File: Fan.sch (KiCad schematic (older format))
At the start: 0 parts

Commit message: Completed LED Driver Video + Power Module
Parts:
- added Q?: MOSFET_N, ~, symbol MOSFET_N
- added R? (x5): R, ~, symbol R
- added RV?: POT, ~, symbol POT
- added U?: LM324, symbol LM324
- added U?: MCP4922-E/P, DIP14, symbol MCP4922-E/P
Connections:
- net labels added: +12V, -12V, AGND, CS_N, Current Measure, MISO, MOSI, SCLK
- wire segments 0 -> 32
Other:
- note added: "NEED TO CHANGE CS NAME, THIS WILL DUPLICATE WITH THE OTHER CS ON TC"

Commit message: Completed Arduino Module Video
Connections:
- net labels added: CURR_MEAS, FAN_EN_N, FAN_OUT+, FAN_OUT-, TACH_IN, TACH_MEAS
- net labels removed: Current Measure, Fan_In, Power+, Power-, Tach, Tach_Out
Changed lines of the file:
@@
 $Descr A4 11693 8268
 encoding utf-8
-Sheet 7 9
+Sheet 8 9
 Title ""
-Date "10 feb 2014"
+Date "11 feb 2014"
 Rev ""
 Comp ""
@@
 $EndDescr
 Text HLabel 8900 3500 2    60   Output ~ 0
-Power+
-Text HLabel 8900 4000 2    60   Input ~ 0
-Power-
+FAN_OUT+
+Text HLabel 8900 4000 2    60   Output ~ 0
+FAN_OUT-
 Text HLabel 9000 5900 2    60   Input ~ 0
-Tach
+TACH_IN
 Text HLabel 1900 5900 0    60   Output ~ 0
-Tach_Out
+TACH_MEAS
 Text HLabel 1850 4350 0    60   Input ~ 0
-Fan_In
+FAN_EN_N
 $Comp
 L LM324 U?
@@
 Connection ~ 4800 3950
 Text HLabel 2300 4750 0    60   Output ~ 0
-Current Measure
+CURR_MEAS
 Wire Wire Line
 	2300 4750 7950 4750

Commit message: Fan Module Update
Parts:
- removed R? (x2): R, ~, symbol R
- removed RV?: POT, ~, symbol POT
- added D?: DIODE, ~, symbol DIODE
- added Q? (x2): MOSFET_N, ~, symbol MOSFET_N
- added TH?: THERMISTOR, ~, symbol THERMISTOR
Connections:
- net labels added: +12C, FAN_MODE, FAN_PWM
- net labels removed: FAN_EN_N
- wire segments 32 -> 42
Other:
- moved on the sheet: R?
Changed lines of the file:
@@
 Comment4 ""
 $EndDescr
-Text HLabel 8900 3500 2    60   Output ~ 0
+Text HLabel 9450 2350 2    60   Output ~ 0
 FAN_OUT+
-Text HLabel 8900 4000 2    60   Output ~ 0
+Text HLabel 9450 2950 2    60   Output ~ 0
 FAN_OUT-
-Text HLabel 9000 5900 2    60   Input ~ 0
+Text HLabel 8900 6950 2    60   Input ~ 0
 TACH_IN
-Text HLabel 1900 5900 0    60   Output ~ 0
+Text HLabel 1800 6950 0    60   Output ~ 0
 TACH_MEAS
 Text HLabel 1850 4350 0    60   Input ~ 0
-FAN_EN_N
+FAN_PWM
 $Comp
 L LM324 U?
@@
 $EndComp
 $Comp
-L +12V #PWR?
-U 1 1 52F64FC8
-P 7950 2450
-F 0 "#PWR?" H 7950 2400 20  0001 C CNN
-F 1 "+12V" H 7950 2550 30  0000 C CNN
-F 2 "" H 7950 2450 60  0000 C CNN
-F 3 "" H 7950 2450 60  0000 C CNN
-	1    7950 2450
-	1    0    0    -1
-$EndComp
-$Comp
 L AGND #PWR?
 U 1 1 52F64FE1
-P 7950 5600
-F 0 "#PWR?" H 7950 5600 40  0001 C CNN
-F 1 "AGND" H 7950 5530 50  0000 C CNN
-F 2 "" H 7950 5600 60  0000 C CNN
-F 3 "" H 7950 5600 60  0000 C CNN
-	1    7950 5600
+P 7950 6100
+F 0 "#PWR?" H 7950 6100 40  0001 C CNN
+F 1 "AGND" H 7950 6030 50  0000 C CNN
+F 2 "" H 7950 6100 60  0000 C CNN
+F 3 "" H 7950 6100 60  0000 C CNN
+	1    7950 6100
 	1    0    0    -1
 $EndComp
@@
 	7650 3250 6950 3250
 Wire Wire Line
-	7950 3450 7950 3500
-Wire Wire Line
-	7950 3500 8900 3500
-Wire Wire Line
-	5750 4000 8900 4000
-Wire Wire Line
-	7950 4000 7950 4900
+	7950 3450 7950 4000
+Wire Wire Line
+	7950 4000 7950 4750
+Wire Wire Line
+	7950 4750 7950 5000
+Wire Wire Line
+	7950 5000 7950 5150
 $Comp
 L R R?
 U 1 1 52F65013
-P 7950 5150
-F 0 "R?" V 8030 5150 40  0000 C CNN
-F 1 "R" V 7957 5151 40  0000 C CNN
-F 2 "~" V 7880 5150 30  0000 C CNN
-F 3 "~" H 7950 5150 30  0000 C CNN
-	1    7950 5150
-	1    0    0    -1
-$EndComp
-Wire Wire Line
-	7950 5400 7950 5600
-Wire Wire Line
-	7950 3050 7950 2450
+P 7950 5400
+F 0 "R?" V 8030 5400 40  0000 C CNN
+F 1 "R" V 7957 5401 40  0000 C CNN
+F 2 "~" V 7880 5400 30  0000 C CNN
+F 3 "~" H 7950 5400 30  0000 C CNN
+	1    7950 5400
+	1    0    0    -1
+$EndComp
+Wire Wire Line
+	7950 5650 7950 5850
+Wire Wire Line
+	7950 5850 7950 6100
 Wire Wire Line
 	5750 4000 5750 3350
 Wire Wire Line
 	5750 3350 5950 3350
-Connection ~ 7950 4000
 $Comp
 L +12V #PWR?
@@
 $EndComp
 $Comp
-L R R?
-U 1 1 52F651D7
-P 4800 2800
-F 0 "R?" V 4880 2800 40  0000 C CNN
-F 1 "R" V 4807 2801 40  0000 C CNN
-F 2 "~" V 4730 2800 30  0000 C CNN
-F 3 "~" H 4800 2800 30  0000 C CNN
-	1    4800 2800
-	1    0    0    -1
-$EndComp
-Wire Wire Line
-	4800 3050 4800 3350
-$Comp
-L +12V #PWR?
-U 1 1 52F651EE
-P 4800 2450
-F 0 "#PWR?" H 4800 2400 20  0001 C CNN
-F 1 "+12V" H 4800 2550 30  0000 C CNN
-F 2 "" H 4800 2450 60  0000 C CNN
-F 3 "" H 4800 2450 60  0000 C CNN
-	1    4800 2450
-	1    0    0    -1
-$EndComp
-Wire Wire Line
-	4800 2550 4800 2450
-$Comp
-L POT RV?
-U 1 1 52F65207
-P 4800 3600
-F 0 "RV?" H 4800 3500 50  0000 C CNN
-F 1 "POT" H 4800 3600 50  0000 C CNN
-F 2 "~" H 4800 3600 60  0000 C CNN
-F 3 "~" H 4800 3600 60  0000 C CNN
-	1    4800 3600
-	0    1    1    0
-$EndComp
-$Comp
 L AGND #PWR?
 U 1 1 52F6521E
-P 4800 4150
-F 0 "#PWR?" H 4800 4150 40  0001 C CNN
-F 1 "AGND" H 4800 4080 50  0000 C CNN
-F 2 "" H 4800 4150 60  0000 C CNN
-F 3 "" H 4800 4150 60  0000 C CNN
-	1    4800 4150
-	1    0    0    -1
-$EndComp
-Wire Wire Line
-	4800 3850 4800 4150
-Connection ~ 4800 3150
-Wire Wire Line
-	4950 3600 5050 3600
-Wire Wire Line
-	5050 3600 5050 3950
-Wire Wire Line
-	5050 3950 4800 3950
-Connection ~ 4800 3950
-Text HLabel 2300 4750 0    60   Output ~ 0
+P 5100 4150
+F 0 "#PWR?" H 5100 4150 40  0001 C CNN
+F 1 "AGND" H 5100 4080 50  0000 C CNN
+F 2 "" H 5100 4150 60  0000 C CNN
+F 3 "" H 5100 4150 60  0000 C CNN
+	1    5100 4150
+	1    0    0    -1
+$EndComp
+Text HLabel 1850 4750 0    60   Output ~ 0
 CURR_MEAS
 Wire Wire Line
-	2300 4750 7950 4750
+	1850 4750 7950 4750
 Connection ~ 7950 4750
 Text HLabel 1150 3100 0    60   Input ~ 0
@@
 NEED TO CHANGE CS NAME,  THIS WILL DUPLICATE WITH THE OTHER CS ON TC
 Wire Wire Line
-	1900 5900 9000 5900
+	1800 6950 8900 6950
 $Comp
 L R R?
@@
 Wire Wire Line
 	1850 4350 2850 4350
-Wire Wire Line
-	5400 4350 3350 4350
-Connection ~ 5400 3150
 $Comp
 L R R?
@@
 	3150 3150 3750 3150
 Wire Wire Line
-	4250 3150 5950 3150
-Wire Wire Line
-	5400 3150 5400 4350
-$Comp
-L R R?
-U 1 1 52F654DF
-P 1950 3950
-F 0 "R?" V 2030 3950 40  0000 C CNN
-F 1 "R" V 1957 3951 40  0000 C CNN
-F 2 "~" V 1880 3950 30  0000 C CNN
-F 3 "~" H 1950 3950 30  0000 C CNN
-	1    1950 3950
-	-1   0    0    1
-$EndComp
-Wire Wire Line
-	1950 3700 1950 3500
-Wire Wire Line
-	1950 3500 2050 3500
-Wire Wire Line
-	1950 4200 1950 4350
-Connection ~ 1950 4350
+	4250 3150 5100 3150
+Wire Wire Line
+	5100 3150 5950 3150
+$Comp
+L THERMISTOR TH?
+U 1 1 52FA45CA
+P 7950 2050
+F 0 "TH?" V 8050 2100 50  0000 C CNN
+F 1 "THERMISTOR" V 7850 2050 50  0000 C CNN
+F 2 "~" H 7950 2050 60  0000 C CNN
+F 3 "~" H 7950 2050 60  0000 C CNN
+	1    7950 2050
+	1    0    0    -1
+$EndComp
+Wire Wire Line
+	7950 1800 7950 1600
+Wire Wire Line
+	7950 2300 7950 2350
+Wire Wire Line
+	7550 2350 7950 2350
+Wire Wire Line
+	7950 2350 9450 2350
+Wire Wire Line
+	7550 2950 7950 2950
+Wire Wire Line
+	7950 2950 9450 2950
+Wire Wire Line
+	7950 2950 7950 3050
+$Comp
+L DIODE D?
+U 1 1 52FA4653
+P 7550 2650
+F 0 "D?" H 7550 2750 40  0000 C CNN
+F 1 "DIODE" H 7550 2550 40  0000 C CNN
+F 2 "~" H 7550 2650 60  0000 C CNN
+F 3 "~" H 7550 2650 60  0000 C CNN
+	1    7550 2650
+	0    -1   -1   0
+$EndComp
+Wire Wire Line
+	7550 2850 7550 2950
+Connection ~ 7950 2950
+Wire Wire Line
+	7550 2450 7550 2350
+Connection ~ 7950 2350
+$Comp
+L MOSFET_N Q?
+U 1 1 52FA4715
+P 7300 5400
+F 0 "Q?" H 7310 5570 60  0000 R CNN
+F 1 "MOSFET_N" H 7310 5250 60  0000 R CNN
+F 2 "~" H 7300 5400 60  0000 C CNN
+F 3 "~" H 7300 5400 60  0000 C CNN
+	1    7300 5400
+	1    0    0    -1
+$EndComp
+Wire Wire Line
+	7400 5200 7400 5000
+Wire Wire Line
+	7400 5000 7950 5000
+Connection ~ 7950 5000
+Wire Wire Line
+	7400 5600 7400 5850
+Wire Wire Line
+	7400 5850 7950 5850
+Connection ~ 7950 5850
+Wire Wire Line
+	5750 4000 7950 4000
+Connection ~ 7950 4000
+$Comp
+L MOSFET_N Q?
+U 1 1 52FA47D3
+P 5000 3700
+F 0 "Q?" H 5010 3870 60  0000 R CNN
+F 1 "MOSFET_N" H 5010 3550 60  0000 R CNN
+F 2 "~" H 5000 3700 60  0000 C CNN
+F 3 "~" H 5000 3700 60  0000 C CNN
+	1    5000 3700
+	1    0    0    -1
+$EndComp
+Wire Wire Line
+	5100 3500 5100 3150
+Connection ~ 5100 3150
+Wire Wire Line
+	5100 3900 5100 4150
+Wire Wire Line
+	3350 4350 4000 4350
+Wire Wire Line
+	4000 4350 4000 3700
+Wire Wire Line
+	4000 3700 4800 3700
+Text HLabel 1850 5400 0    60   Input ~ 0
+FAN_MODE
+Wire Wire Line
+	1850 5400 7100 5400
+$Comp
+L +12C #PWR?
+U 1 1 52FA51D6
+P 7950 1600
+F 0 "#PWR?" H 7950 1570 30  0001 C CNN
+F 1 "+12C" H 7950 1710 40  0000 C CNN
+F 2 "" H 7950 1600 60  0000 C CNN
+F 3 "" H 7950 1600 60  0000 C CNN
+	1    7950 1600
+	1    0    0    -1
+$EndComp
 $EndSCHEMATC

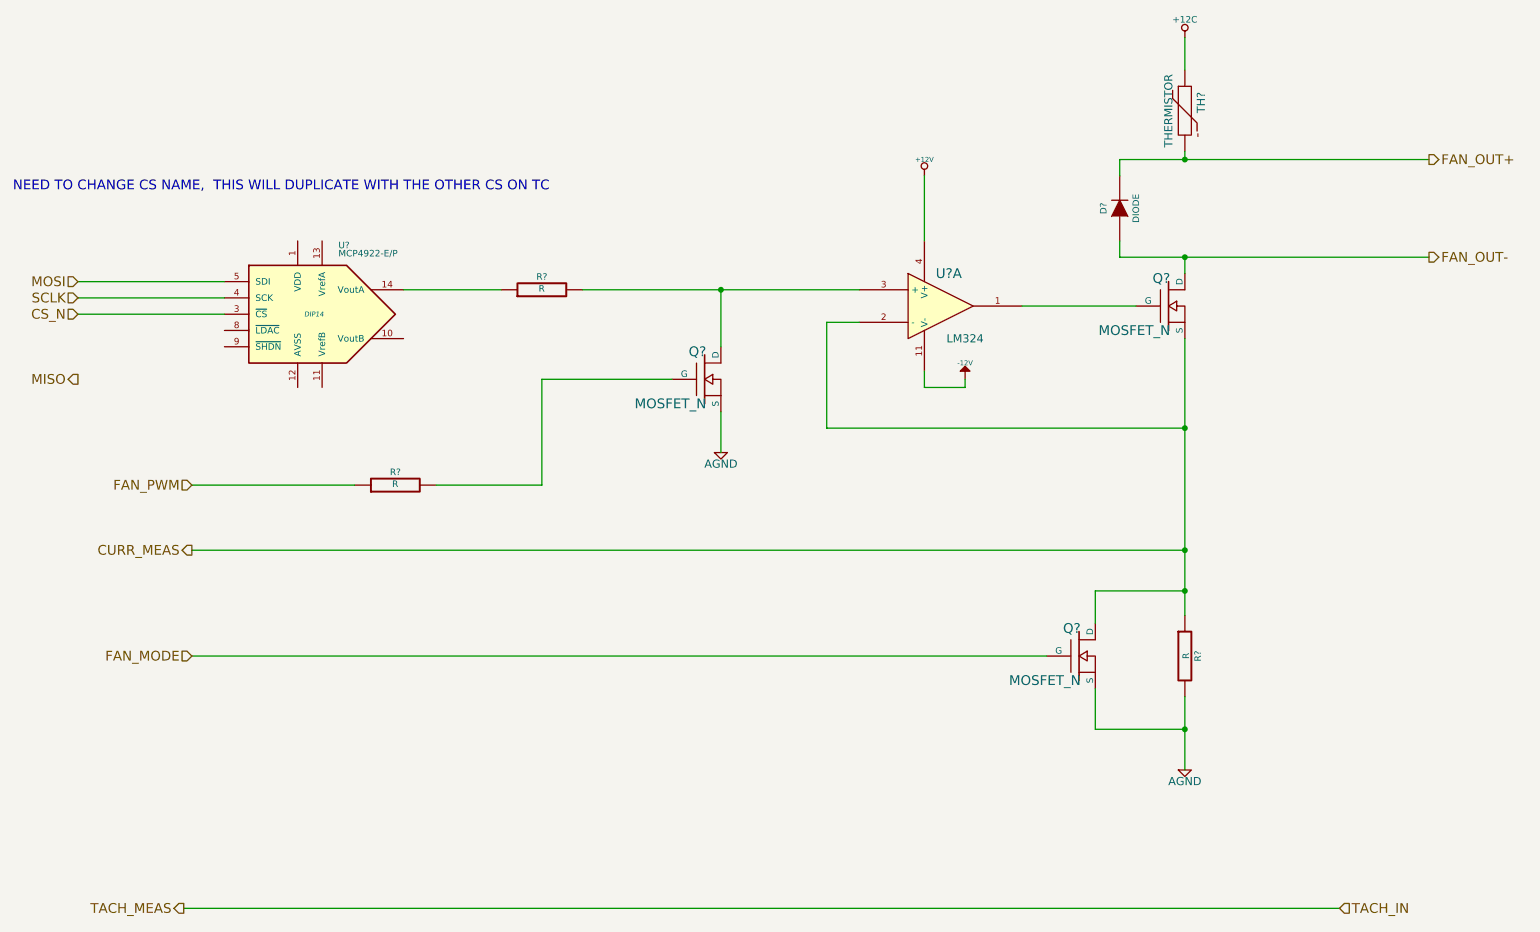
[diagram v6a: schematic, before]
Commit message: started associating relay parts
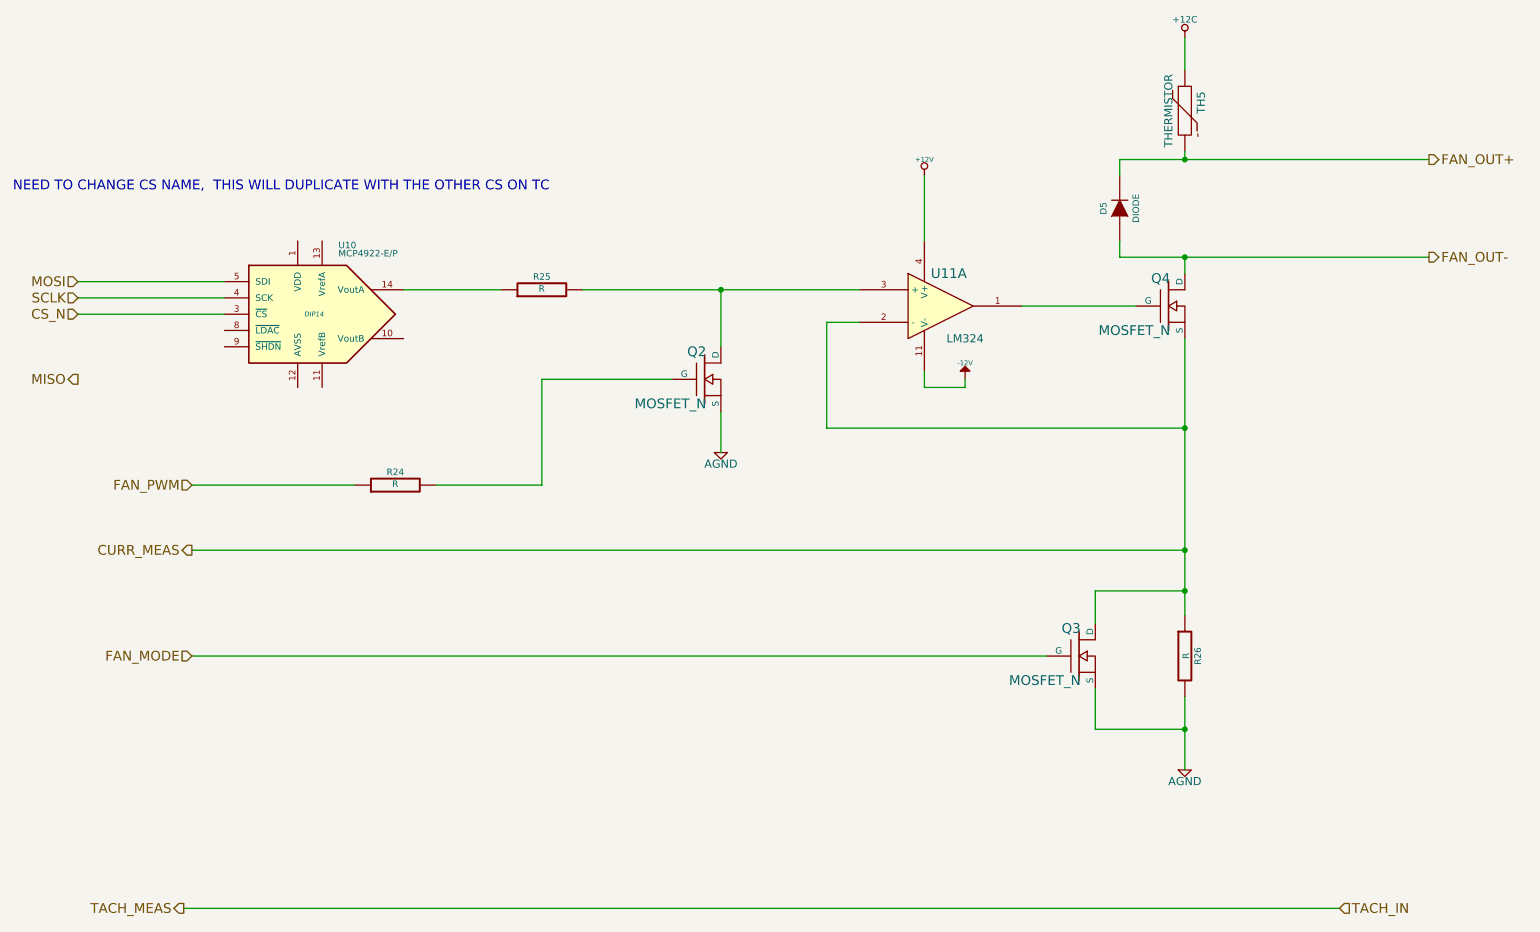
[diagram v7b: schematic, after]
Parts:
- gave numbers to parts that had none: 10
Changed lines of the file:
@@
 Sheet 8 9
 Title ""
-Date "17 feb 2014"
+Date "20 feb 2014"
 Rev ""
 Comp ""
@@
 FAN_PWM
 $Comp
-L LM324 U?
+L LM324 U11
 U 1 1 52F64FAA
 P 6450 3250
-F 0 "U?" H 6500 3450 60  0000 C CNN
+F 0 "U11" H 6500 3450 60  0000 C CNN
 F 1 "LM324" H 6600 3050 50  0000 C CNN
 F 2 "" H 6450 3250 60  0000 C CNN
@@
 $EndComp
 $Comp
-L MOSFET_N Q?
+L MOSFET_N Q4
 U 1 1 52F64FB9
 P 7850 3250
-F 0 "Q?" H 7860 3420 60  0000 R CNN
+F 0 "Q4" H 7860 3420 60  0000 R CNN
 F 1 "MOSFET_N" H 7860 3100 60  0000 R CNN
 F 2 "~" H 7850 3250 60  0000 C CNN
@@
 $EndComp
 $Comp
-L AGND #PWR?
+L AGND #PWR041
 U 1 1 52F64FE1
 P 7950 6100
-F 0 "#PWR?" H 7950 6100 40  0001 C CNN
+F 0 "#PWR041" H 7950 6100 40  0001 C CNN
 F 1 "AGND" H 7950 6030 50  0000 C CNN
 F 2 "" H 7950 6100 60  0000 C CNN
@@
 	7650 3250 6950 3250
 Wire Wire Line
-	7950 3450 7950 4000
-Wire Wire Line
-	7950 4000 7950 4750
-Wire Wire Line
-	7950 4750 7950 5000
-Wire Wire Line
-	7950 5000 7950 5150
-$Comp
-L R R?
+	7950 3450 7950 5150
+$Comp
+L R R26
 U 1 1 52F65013
 P 7950 5400
-F 0 "R?" V 8030 5400 40  0000 C CNN
+F 0 "R26" V 8030 5400 40  0000 C CNN
 F 1 "R" V 7957 5401 40  0000 C CNN
 F 2 "~" V 7880 5400 30  0000 C CNN
@@
 $EndComp
 Wire Wire Line
-	7950 5650 7950 5850
-Wire Wire Line
-	7950 5850 7950 6100
+	7950 5650 7950 6100
 Wire Wire Line
 	5750 4000 5750 3350
@@
 	5750 3350 5950 3350
 $Comp
-L +12V #PWR?
+L +12V #PWR042
 U 1 1 52F65053
 P 6350 2450
-F 0 "#PWR?" H 6350 2400 20  0001 C CNN
+F 0 "#PWR042" H 6350 2400 20  0001 C CNN
 F 1 "+12V" H 6350 2550 30  0000 C CNN
 F 2 "" H 6350 2450 60  0000 C CNN
@@
 	6350 2450 6350 2850
 $Comp
-L -12V #PWR?
+L -12V #PWR043
 U 1 1 52F65100
 P 6600 3700
-F 0 "#PWR?" H 6600 3830 20  0001 C CNN
+F 0 "#PWR043" H 6600 3830 20  0001 C CNN
 F 1 "-12V" H 6600 3800 30  0000 C CNN
 F 2 "" H 6600 3700 60  0000 C CNN
@@
 	6600 3750 6600 3700
 $Comp
-L MCP4922-E/P U?
+L MCP4922-E/P U10
 U 1 1 52F651B6
 P 2600 3300
-F 0 "U?" H 2750 3700 40  0000 L BNN
+F 0 "U10" H 2750 3700 40  0000 L BNN
 F 1 "MCP4922-E/P" H 2750 3650 40  0000 L BNN
 F 2 "DIP14" H 2600 3300 30  0000 C CIN
@@
 $EndComp
 $Comp
-L AGND #PWR?
+L AGND #PWR044
 U 1 1 52F6521E
 P 5100 4150
-F 0 "#PWR?" H 5100 4150 40  0001 C CNN
+F 0 "#PWR044" H 5100 4150 40  0001 C CNN
 F 1 "AGND" H 5100 4080 50  0000 C CNN
 F 2 "" H 5100 4150 60  0000 C CNN
@@
 	1800 6950 8900 6950
 $Comp
-L R R?
+L R R24
 U 1 1 52F65324
 P 3100 4350
-F 0 "R?" V 3180 4350 40  0000 C CNN
+F 0 "R24" V 3180 4350 40  0000 C CNN
 F 1 "R" V 3107 4351 40  0000 C CNN
 F 2 "~" V 3030 4350 30  0000 C CNN
@@
 	1850 4350 2850 4350
 $Comp
-L R R?
+L R R25
 U 1 1 52F6536C
 P 4000 3150
-F 0 "R?" V 4080 3150 40  0000 C CNN
+F 0 "R25" V 4080 3150 40  0000 C CNN
 F 1 "R" V 4007 3151 40  0000 C CNN
 F 2 "~" V 3930 3150 30  0000 C CNN
@@
 	3150 3150 3750 3150
 Wire Wire Line
-	4250 3150 5100 3150
-Wire Wire Line
-	5100 3150 5950 3150
-$Comp
-L THERMISTOR TH?
+	4250 3150 5950 3150
+$Comp
+L THERMISTOR TH5
 U 1 1 52FA45CA
 P 7950 2050
-F 0 "TH?" V 8050 2100 50  0000 C CNN
+F 0 "TH5" V 8050 2100 50  0000 C CNN
 F 1 "THERMISTOR" V 7850 2050 50  0000 C CNN
 F 2 "~" H 7950 2050 60  0000 C CNN
@@
 	7950 2300 7950 2350
 Wire Wire Line
-	7550 2350 7950 2350
-Wire Wire Line
-	7950 2350 9450 2350
-Wire Wire Line
-	7550 2950 7950 2950
-Wire Wire Line
-	7950 2950 9450 2950
+	7550 2350 9450 2350
+Wire Wire Line
+	7550 2950 9450 2950
 Wire Wire Line
 	7950 2950 7950 3050
 $Comp
-L DIODE D?
+L DIODE D5
 U 1 1 52FA4653
 P 7550 2650
-F 0 "D?" H 7550 2750 40  0000 C CNN
+F 0 "D5" H 7550 2750 40  0000 C CNN
 F 1 "DIODE" H 7550 2550 40  0000 C CNN
 F 2 "~" H 7550 2650 60  0000 C CNN
@@
 Connection ~ 7950 2350
 $Comp
-L MOSFET_N Q?
+L MOSFET_N Q3
 U 1 1 52FA4715
 P 7300 5400
-F 0 "Q?" H 7310 5570 60  0000 R CNN
+F 0 "Q3" H 7310 5570 60  0000 R CNN
 F 1 "MOSFET_N" H 7310 5250 60  0000 R CNN
 F 2 "~" H 7300 5400 60  0000 C CNN
@@
 Connection ~ 7950 4000
 $Comp
-L MOSFET_N Q?
+L MOSFET_N Q2
 U 1 1 52FA47D3
 P 5000 3700
-F 0 "Q?" H 5010 3870 60  0000 R CNN
+F 0 "Q2" H 5010 3870 60  0000 R CNN
 F 1 "MOSFET_N" H 5010 3550 60  0000 R CNN
 F 2 "~" H 5000 3700 60  0000 C CNN
@@
 	1850 5400 7100 5400
 $Comp
-L +12C #PWR?
+L +12C #PWR045
 U 1 1 52FA51D6
 P 7950 1600
-F 0 "#PWR?" H 7950 1570 30  0001 C CNN
+F 0 "#PWR045" H 7950 1570 30  0001 C CNN
 F 1 "+12C" H 7950 1710 40  0000 C CNN
 F 2 "" H 7950 1600 60  0000 C CNN
